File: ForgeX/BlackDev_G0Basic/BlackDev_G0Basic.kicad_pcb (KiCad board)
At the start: 2 copper layers, 53.9 x 59.4 mm, 10 parts, among them J1 Conn_01x02_Pin, J6 Conn_02x20_Odd_Even

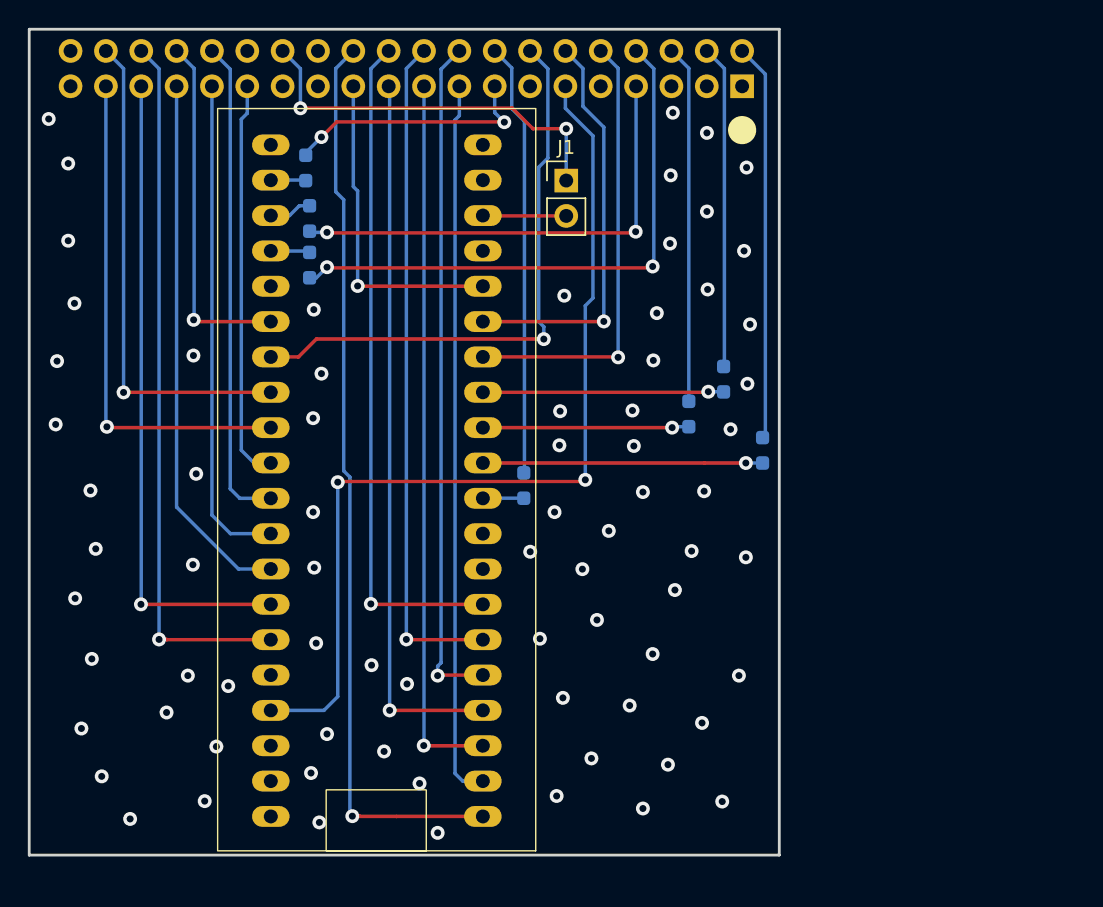
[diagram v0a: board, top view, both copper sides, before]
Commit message: BlackDevG0 Basic communication update
Added Esp32 as an SPI slave allowing for Telemetry, CAN (TWAI) connection , TCP/IP - UDP Logging, SD-CARD based logging, for a seamless R&D experience
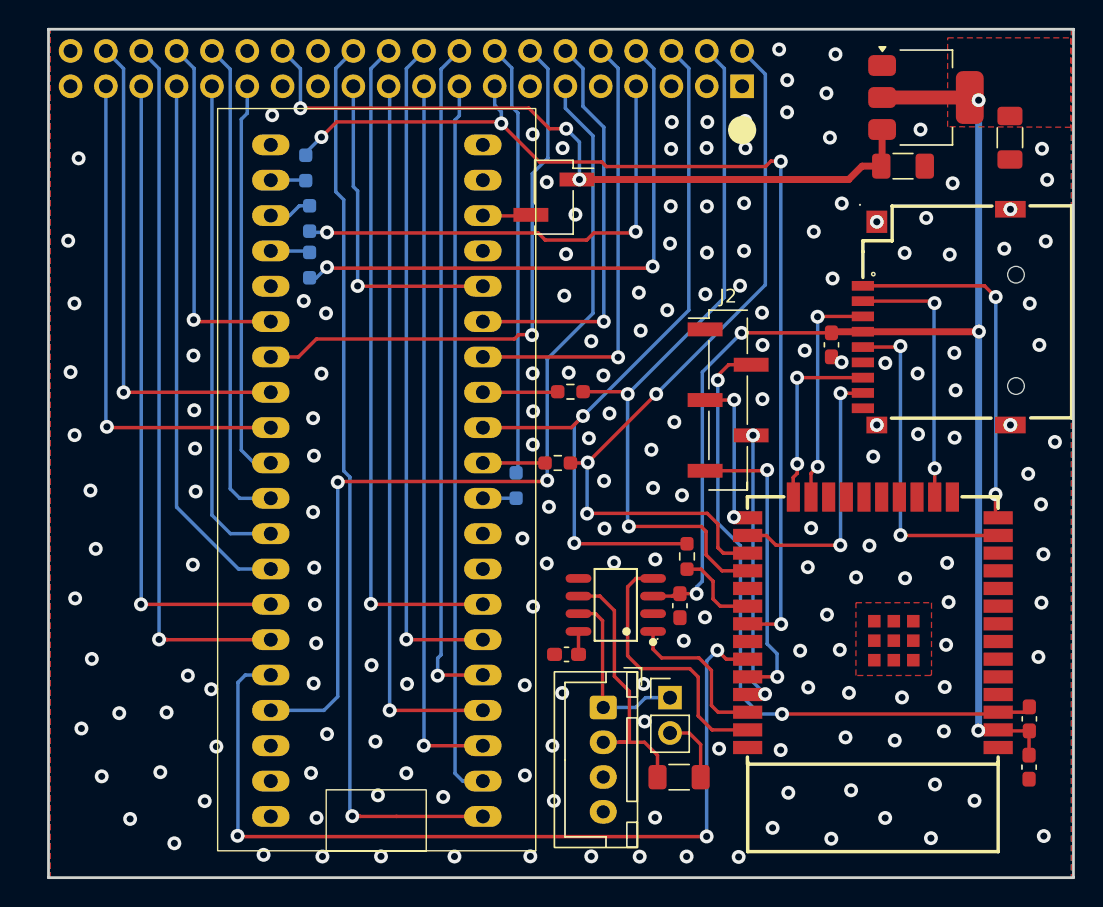
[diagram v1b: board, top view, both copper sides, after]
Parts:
- removed R5: 22, Resistor_SMD:R_0603_1608Metric_Pad0.98x0.95mm_HandSolder
- added C1: 10u, Capacitor_SMD:C_1206_3216Metric_Pad1.33x1.80mm_HandSolder, F.Cu at (197.6, 68.2)
- added C2: 10u, Capacitor_SMD:C_1206_3216Metric_Pad1.33x1.80mm_HandSolder, F.Cu at (189.9, 70.2)
- added C3: 100n, Capacitor_SMD:C_0603_1608Metric_Pad1.08x0.95mm_HandSolder, F.Cu at (173.9, 101.8)
- added C4: 1u, Capacitor_SMD:C_0603_1608Metric_Pad1.08x0.95mm_HandSolder, F.Cu at (198.9, 113.4)
- added C5: 1u, Capacitor_SMD:C_0603_1608Metric_Pad1.08x0.95mm_HandSolder, F.Cu at (184.8, 83.0)
- added J2: PROG, Connector_PinHeader_2.54mm:PinHeader_1x05_P2.54mm_Vertical_SMD_Pin1Left, F.Cu at (177.3, 87.0)
- added J3: Conn_01x02_Pin, Connector_PinHeader_2.54mm:PinHeader_1x02_P2.54mm_Vertical, F.Cu at (173.2, 108.4)
- added J4: Conn_01x04_Pin, Connector_JST:JST_XH_B4B-XH-A_1x04_P2.50mm_Vertical, F.Cu at (168.3, 109.1)
- added R10: 120, Resistor_SMD:R_1206_3216Metric_Pad1.30x1.75mm_HandSolder, F.Cu at (173.8, 114.1)
- added R11: 10k, Capacitor_SMD:C_0603_1608Metric_Pad1.08x0.95mm_HandSolder, F.Cu at (165.7, 105.3)
- added R12: 22, Resistor_SMD:R_0603_1608Metric_Pad0.98x0.95mm_HandSolder, F.Cu at (174.4, 98.2)
- added R9: 10k, Capacitor_SMD:C_0603_1608Metric_Pad1.08x0.95mm_HandSolder, F.Cu at (199.0, 109.9)
- added U2: ESP32-WROOM-32E, EasyEDA:WIFI-SMD_ESP32-WROOM-32E, F.Cu at (187.7, 103.0)
- added U3: AMS1117-3.3, Package_TO_SOT_SMD:SOT-223-3_TabPin2, F.Cu at (191.5, 65.3)
- added U4: SIT65HVD230DR, EasyEDA:SOP-8_L4.9-W3.9-P1.27-LS6.0-BL, F.Cu at (169.2, 101.7)
- added U5: HX TF PUSH, EasyEDA:TF-SMD_TF-PUSH, F.Cu at (192.3, 81.0)
- J1: footprint Connector_PinHeader_2.54mm:PinHeader_1x02_P2.54mm_Vertical -> Connector_PinHeader_2.54mm:PinHeader_1x02_P2.54mm_Vertical_SMD_Pin1Right
- R4, R6: moved to F.Cu
- moved R4 14.7 mm to (165.1, 91.5), turned to 180 degrees
- moved R6 11.0 mm to (166.0, 86.4), turned to 180 degrees
- moved J1 1.49 mm to (164.8, 72.4)
- moved R7 0.55 mm to (162.1, 93.1)
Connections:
- U1 pad 12: Net-(U1-PB4) -> /EXP_MISO
- U1 pad 36: unconnected-(U1-PB2-Pad36) -> /ESP_IRQ
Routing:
- net /3.3V: track 0.00 -> 98.1 mm, vias 0 -> 5
- net /ESP_IRQ: track 0.00 -> 63.5 mm, vias 0 -> 3
- net /EXP_CS2: track 18.2 -> 75.3 mm, vias 2 -> 4
- net /ESP_RST: track 0.00 -> 47.9 mm, vias 0 -> 2
- net /EXP_MISO: track 25.5 -> 55.0 mm, vias 0 -> 2
- net /EXP_MOSI: track 22.8 -> 51.7 mm, vias 0 -> 2
- net /SD_DAT2: track 0.00 -> 25.8 mm, vias 0 -> 2
- net /EXP_SCLK: track 28.5 -> 54.2 mm, vias 0 -> 3
- net /5V: track 28.1 -> 52.9 mm, vias 2 -> 3
- net /SD_CLK: track 0.00 -> 23.3 mm, vias 0 -> 2
- net Net-(J2-Pin_5): track 0.00 -> 21.8 mm, vias 0 -> 2
- net Net-(J2-Pin_4): track 0.00 -> 20.3 mm, vias 0 -> 2
- net /CAN_RXD: track 0.00 -> 19.5 mm
- net /CANL: track 0.00 -> 19.5 mm
- net /SD_DAT1: track 0.00 -> 19.5 mm, vias 0 -> 2
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- added copper zone on F.Cu, net /3.3V
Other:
- board size 53.9 x 59.4 mm -> 73.7 x 61 mm

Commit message: Layout MicroOptimization
More Continous ground, and more orthogonal overlaps in layout
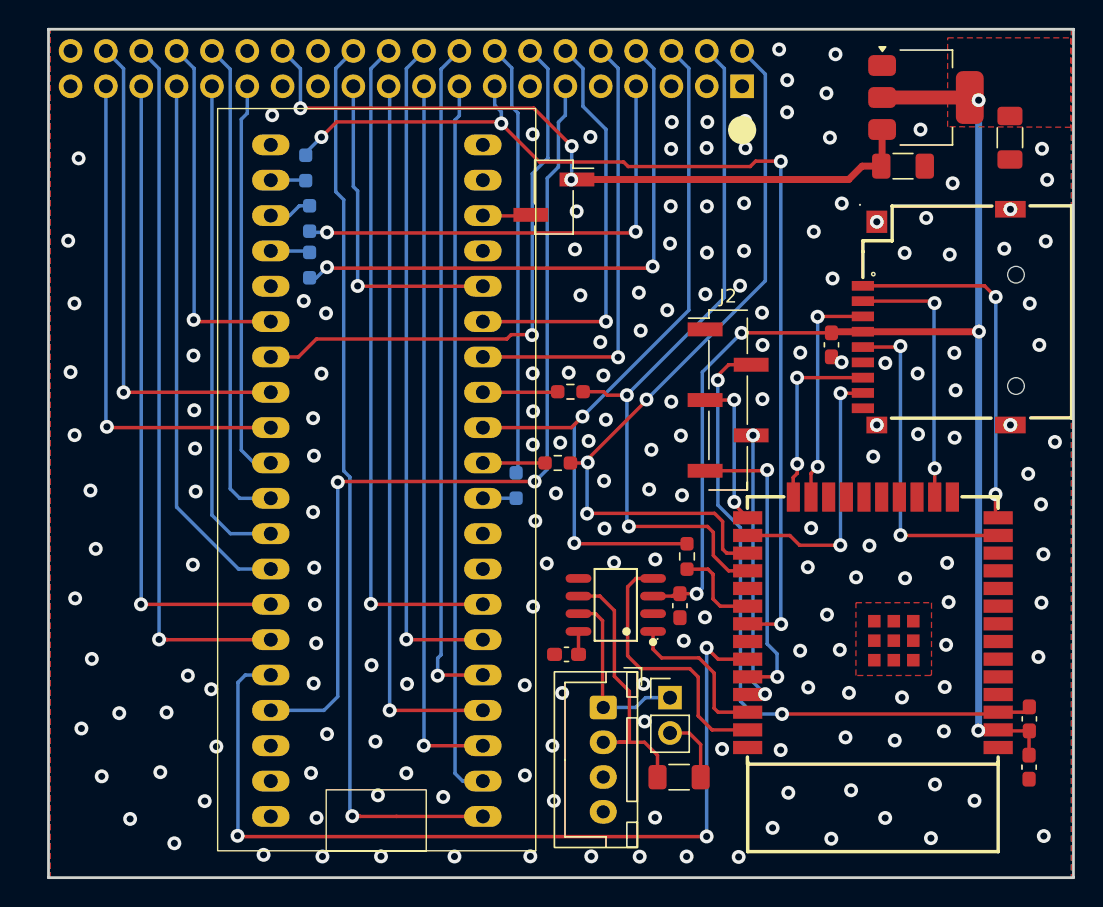
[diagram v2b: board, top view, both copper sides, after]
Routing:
- net /ENC_R3: track 66.2 -> 64.1 mm
- net /ESP_IRQ: track 63.5 -> 64.2 mm
- net /GND: vias 178 -> 179

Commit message: MicroOptimization
Added Teardrops and curved traces
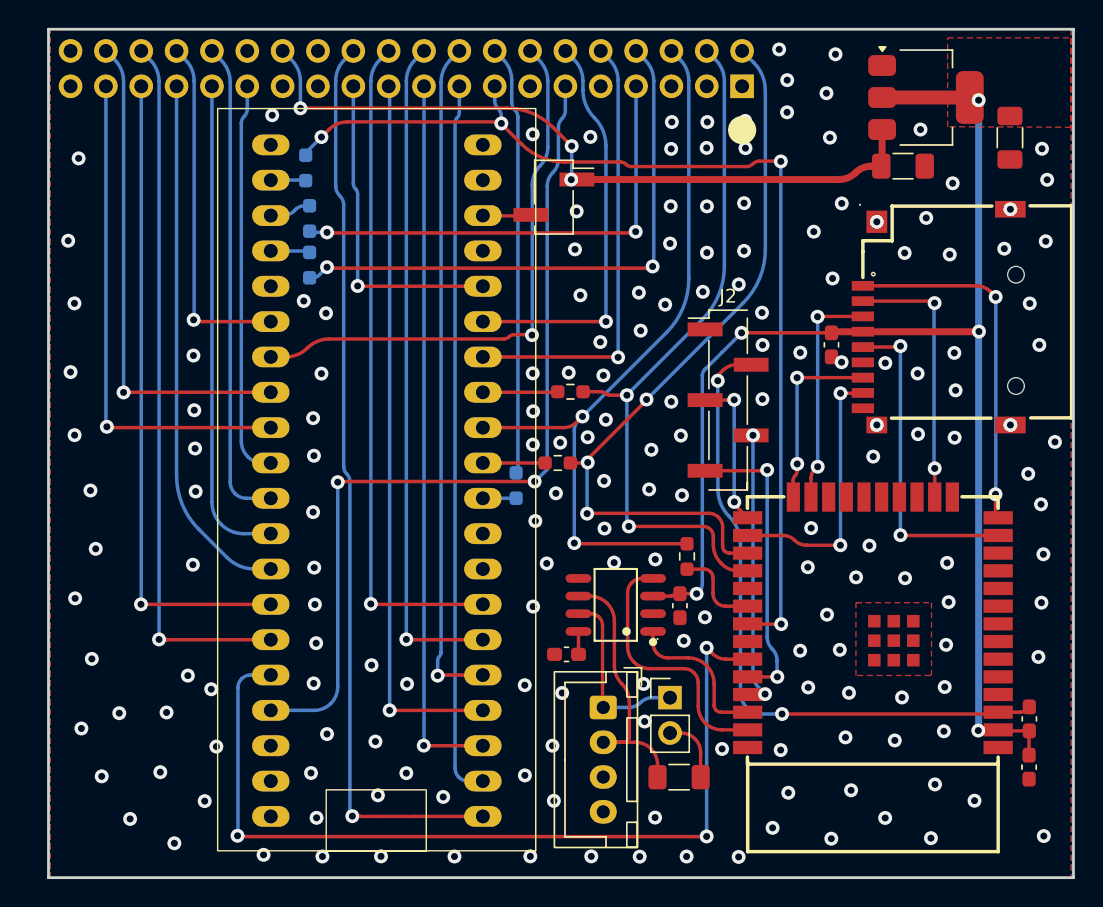
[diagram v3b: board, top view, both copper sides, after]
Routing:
- net /EXP_MOSI: track 51.7 -> 51.1 mm
- net /5V: track 53.2 -> 52.6 mm
- net /EXP_SCLK: track 54.3 -> 53.8 mm
- net /ENC_R2: track 40.9 -> 40.3 mm
- net /ESP_RST: track 48.2 -> 47.6 mm
- net /EXP_CS2: track 75.3 -> 74.8 mm
- net /CAN_RXD: track 19.5 -> 19.0 mm
